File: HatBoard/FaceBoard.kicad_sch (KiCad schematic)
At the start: 18 parts, among them J1 Molex FC Connection, J2 DF11 FC Connection, J3 Conn_01x04, U1 VEML7700, U2 DRV2605LDGS, U25 TMP112AIDRLR, U4 TCA4311A

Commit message: after feedback
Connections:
- net SCLIN: no longer J1.2 (Pin_2), J2.2 (Pin_2), J3.3 (Pin_3), U4.6 (SDAIN)
- new net SDAIN: J1.2 (Pin_2), J2.2 (Pin_2), J3.3 (Pin_3), U4.6 (SDAIN)
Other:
- moved on the sheet: J3

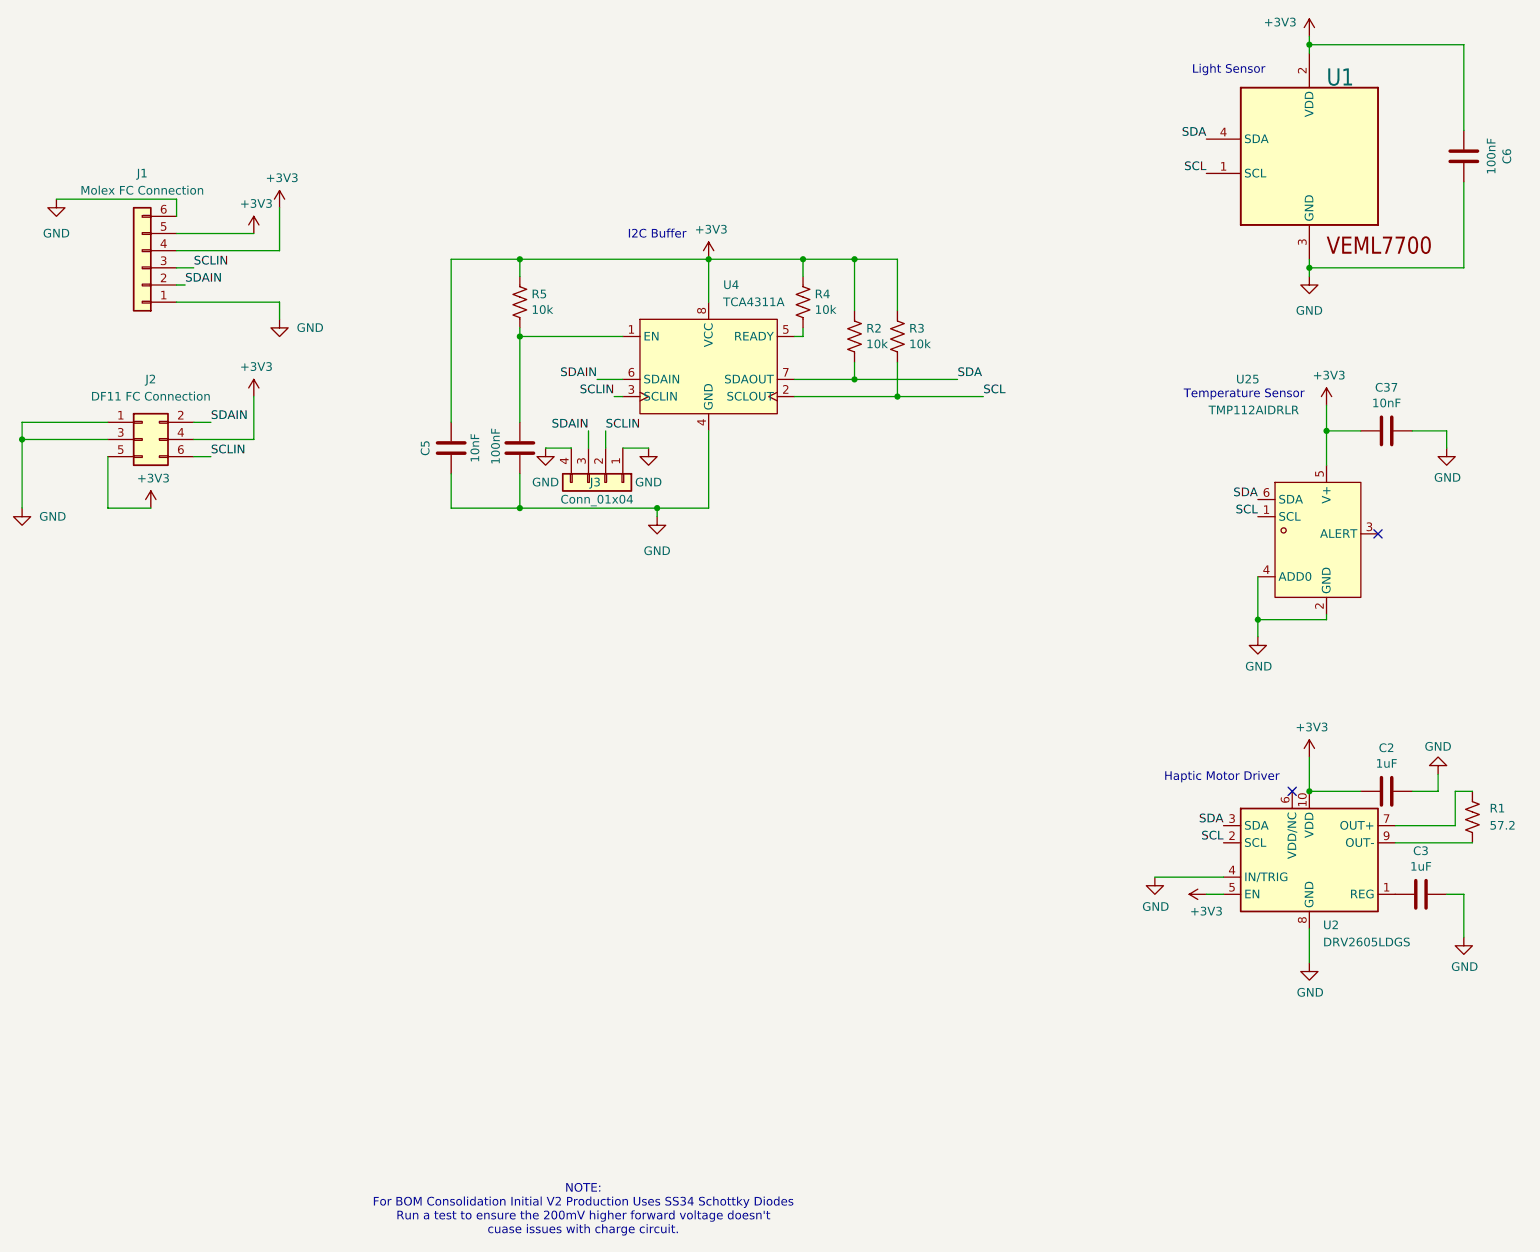
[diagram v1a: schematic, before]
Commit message: changed so only one set of sensors (save money)
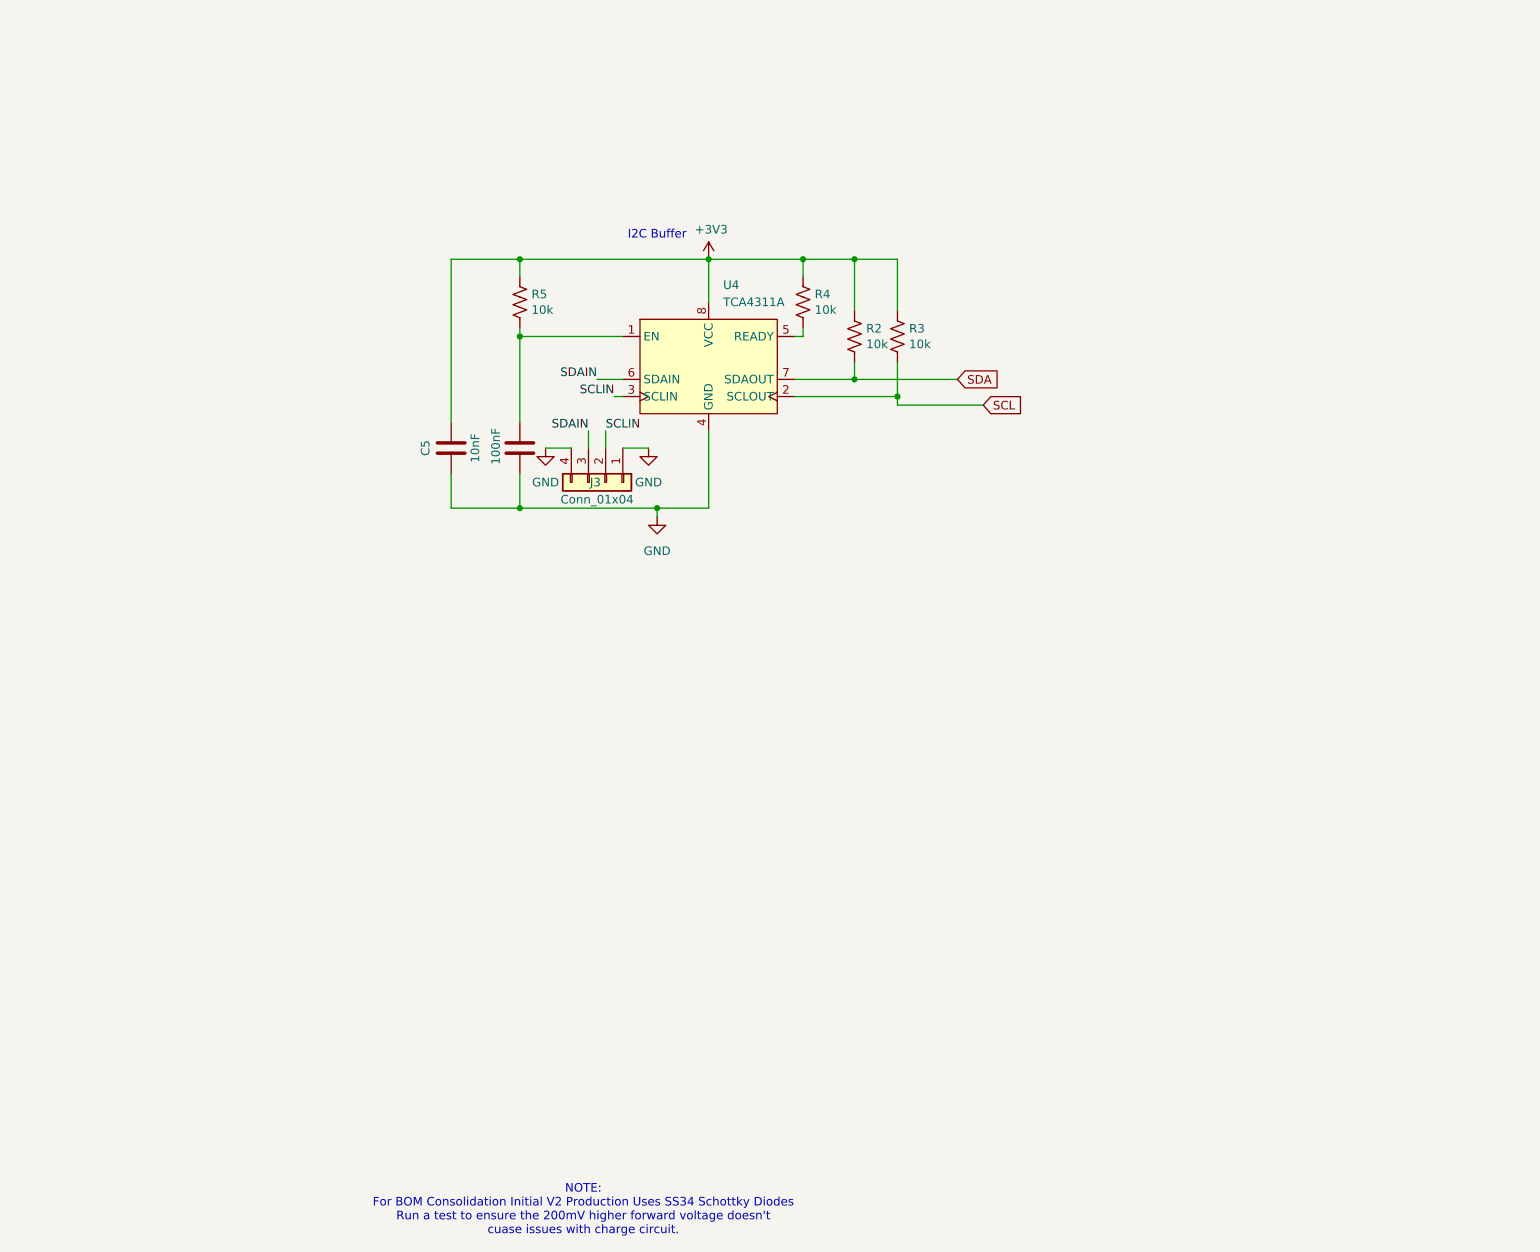
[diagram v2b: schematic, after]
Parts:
- removed C2, C3: 1uF, Capacitor_SMD:C_0805_2012Metric, symbol Device:C
- removed C37: 10nF, Capacitor_SMD:C_0402_1005Metric, symbol Device:C
- removed C6: 100nF, Capacitor_SMD:C_0402_1005Metric, symbol Device:C
- removed J1: Molex FC Connection, easyeda2kicad:CONN-SMD_6P-P1.50_A1501WRB-S-6P, symbol Connector_Generic:Conn_01x06
- removed J2: DF11 FC Connection, Connector_Hirose:Hirose_DF11-6DP-2DSA_2x03_P2.00mm_Vertical, symbol Connector_Generic:Conn_02x03_Odd_Even
- removed R1: 57.2, Resistor_SMD:R_0201_0603Metric_Pad0.64x0.40mm_HandSolder, symbol Device:R_US
- removed U1: VEML7700, easyeda2kicad:SENSOR-SMD_EML7700-TT, symbol Adafruit VEML7700-eagle-import:VEML7700
- removed U2: DRV2605LDGS, Package_SO:VSSOP-10_3x3mm_P0.5mm, symbol Driver_Haptic:DRV2605LDGS
- removed U25: TMP112AIDRLR, easyeda2kicad:SOT-563_L1.6-W1.2-P0.50-LS1.6-BR, symbol easyeda2kicad:TMP112AIDRLR
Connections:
- no-connect marks 2 -> 0
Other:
- note removed: "Haptic Motor Driver"
- note removed: "Light Sensor"
- note removed: "Temperature Sensor"

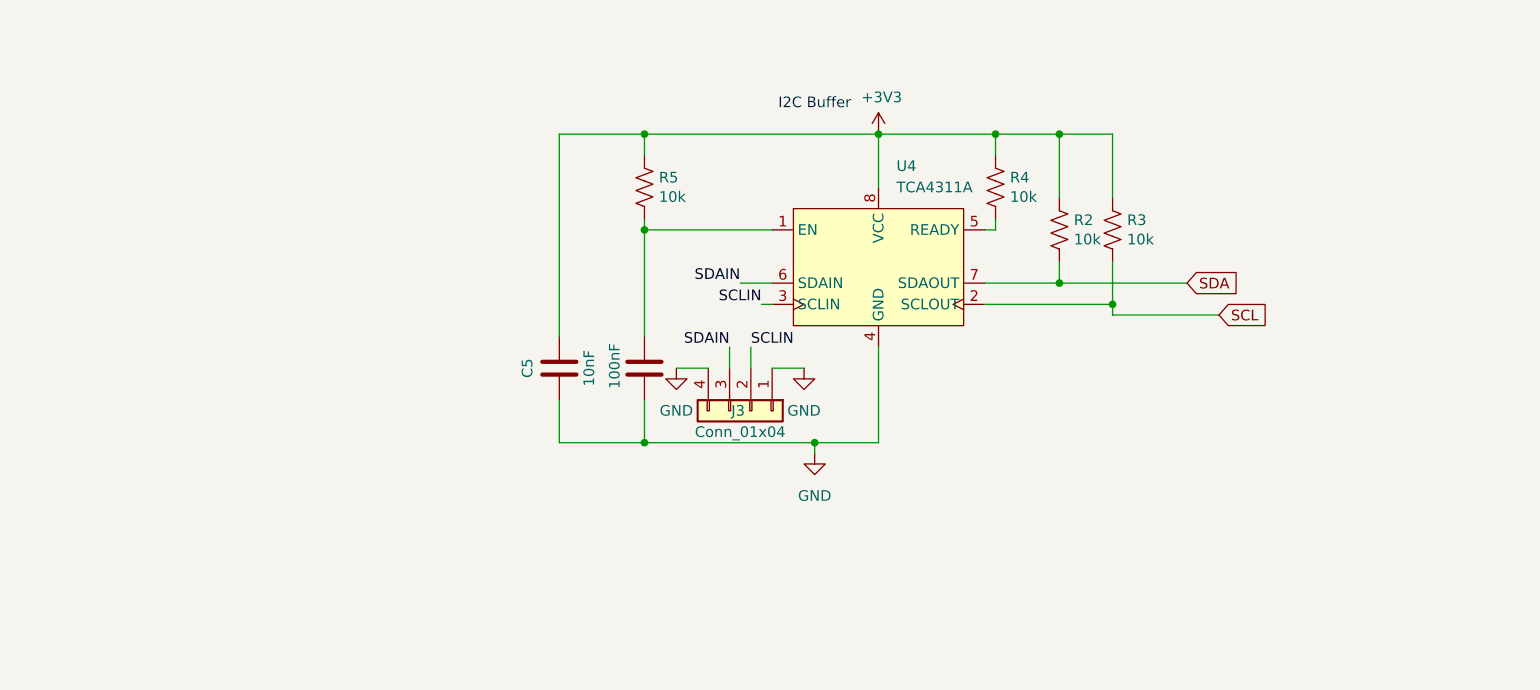
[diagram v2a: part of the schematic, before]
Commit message: changed so only one set of sensors and each has own bus
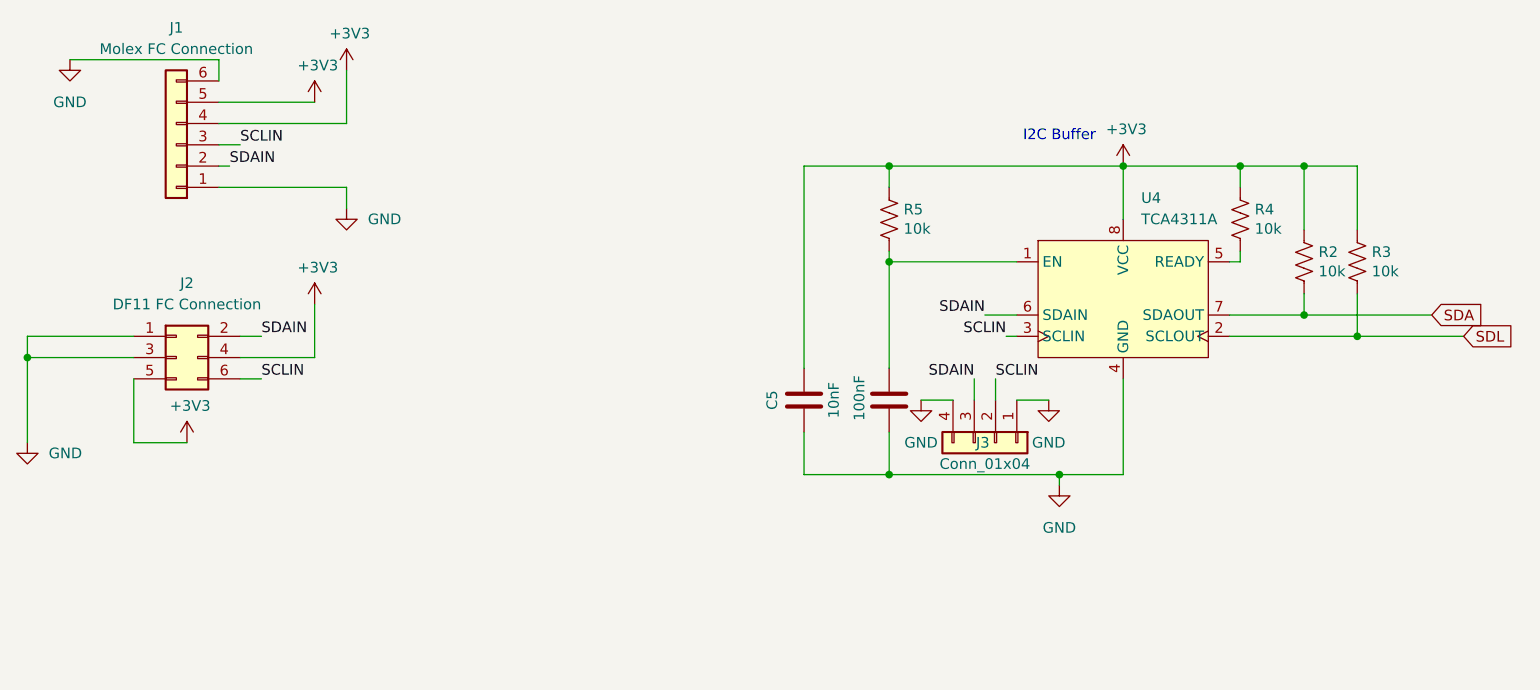
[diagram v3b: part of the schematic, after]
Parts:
- added J1: Molex FC Connection, easyeda2kicad:CONN-SMD_6P-P1.50_A1501WRB-S-6P, symbol Connector_Generic:Conn_01x06
- added J2: DF11 FC Connection, Connector_Hirose:Hirose_DF11-6DP-2DSA_2x03_P2.00mm_Vertical, symbol Connector_Generic:Conn_02x03_Odd_Even
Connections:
- net +3V3: now also J1.4 (Pin_4), J1.5 (Pin_5), J2.4 (Pin_4), J2.5 (Pin_5)
- net GND: now also J1.1 (Pin_1), J1.6 (Pin_6), J2.1 (Pin_1), J2.3 (Pin_3)
- net SCLIN: now also J1.3 (Pin_3), J2.6 (Pin_6)
- net SDAIN: now also J1.2 (Pin_2), J2.2 (Pin_2)
- net SCL renamed SDL
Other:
- moved on the sheet: C5, J3, R2, R3, R4, R5, U4

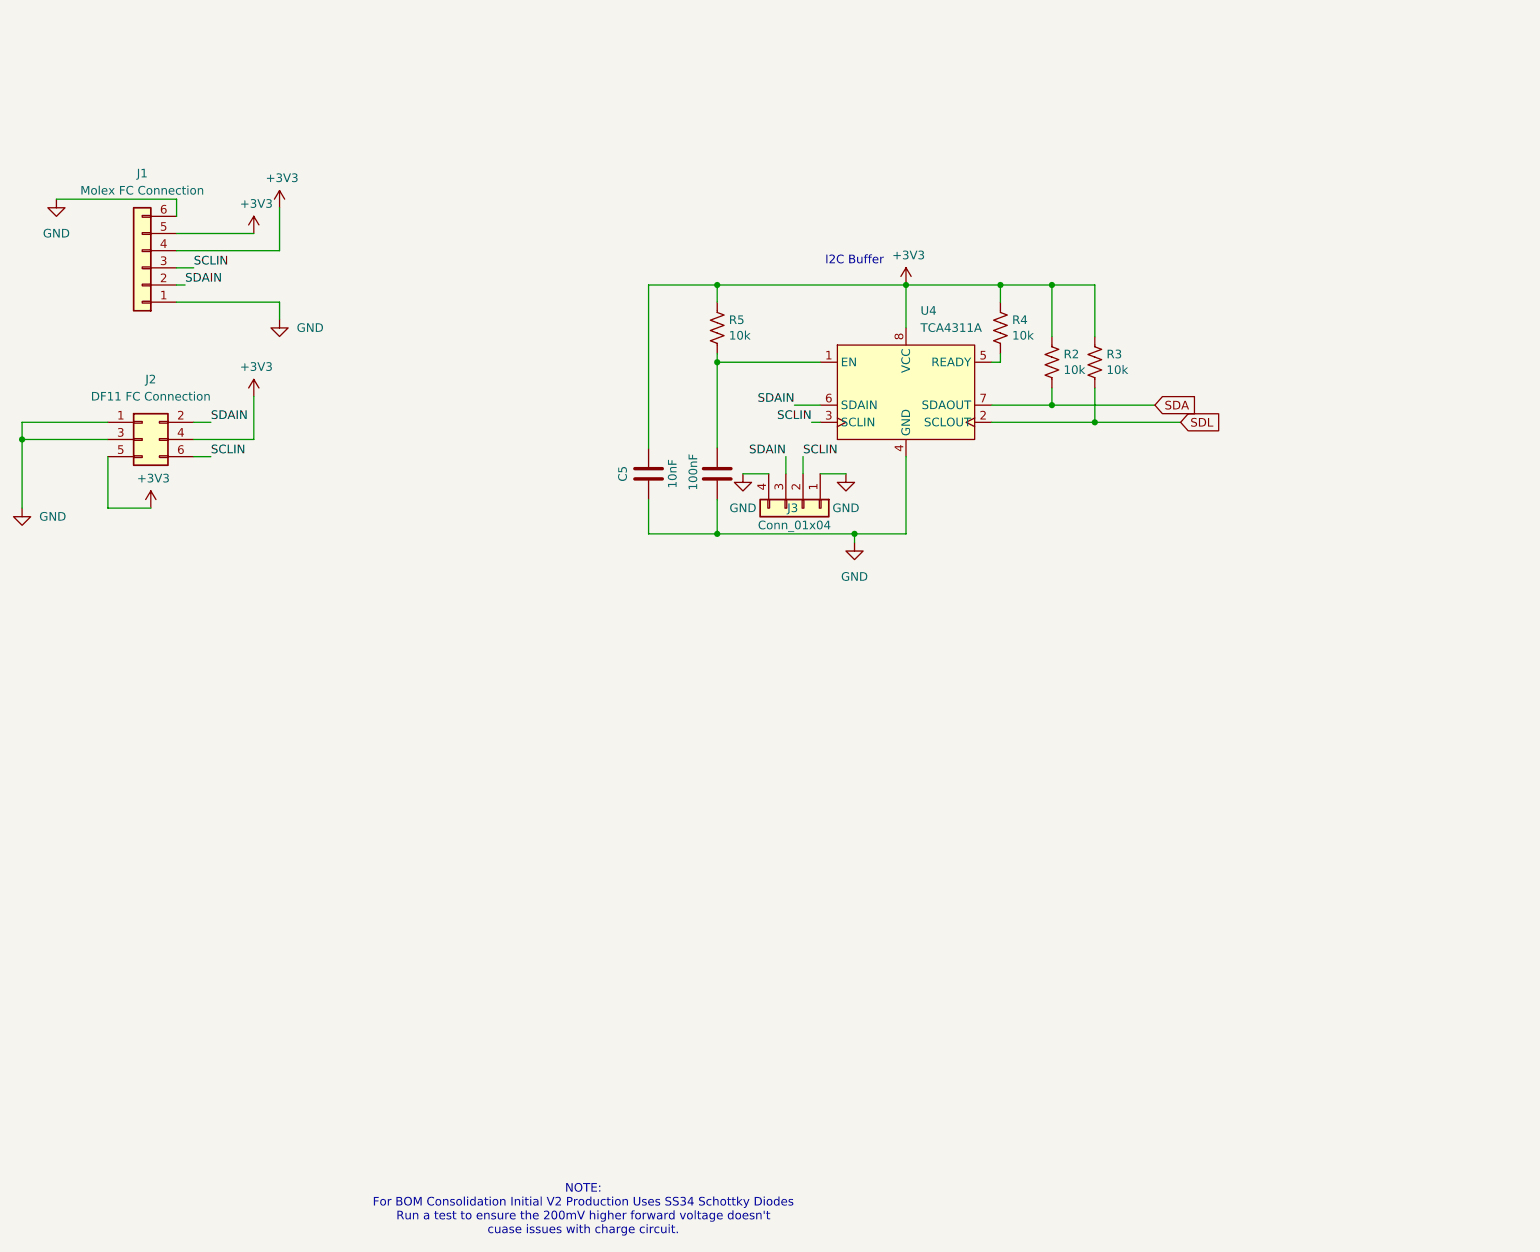
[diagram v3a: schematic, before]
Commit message: fixed the electrical rules checking
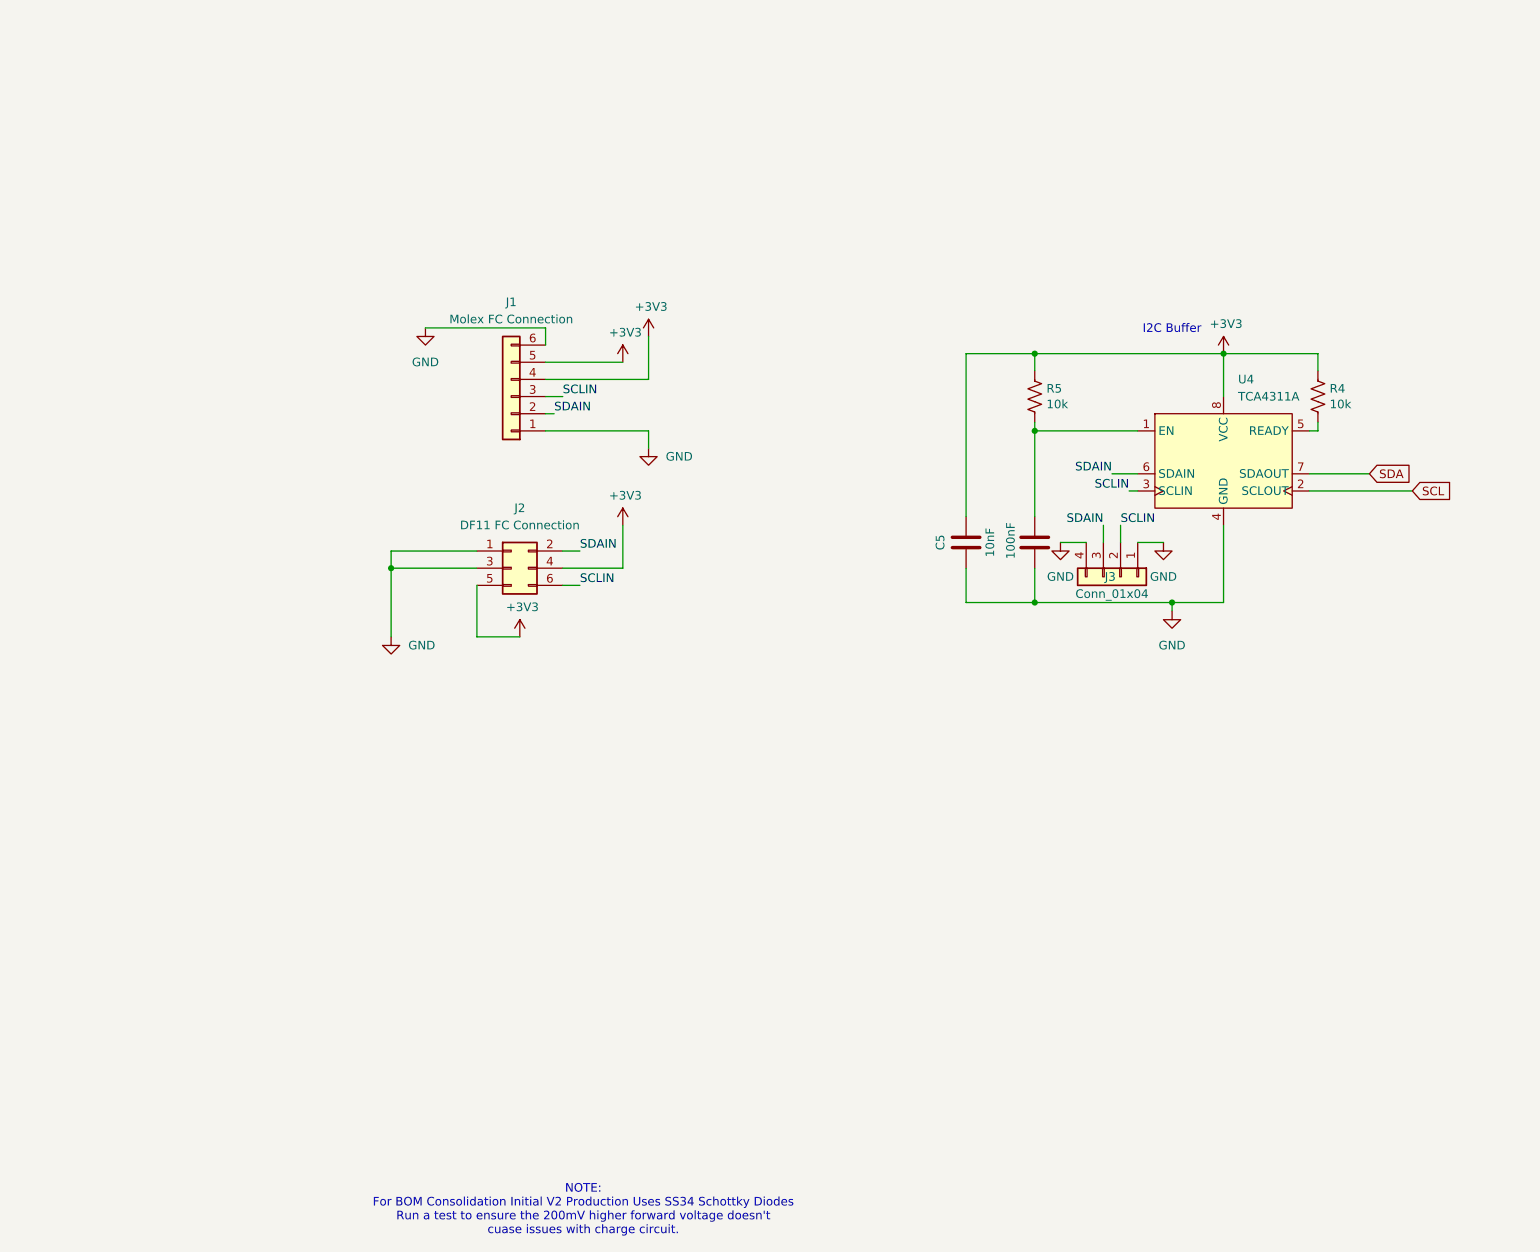
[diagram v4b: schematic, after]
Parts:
- removed R2, R3: 10k, Resistor_SMD:R_0603_1608Metric, symbol Device:R_US
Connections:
- net SDL renamed SCL
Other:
- moved on the sheet: C5, J1, J2, J3, R4, R5, U4
